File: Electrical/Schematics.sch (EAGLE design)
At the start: 16 parts, among them IC1 3V3, IC2 LM358N, J1 HAN Port, J2 Power Supply (5-12V), T1 BC337

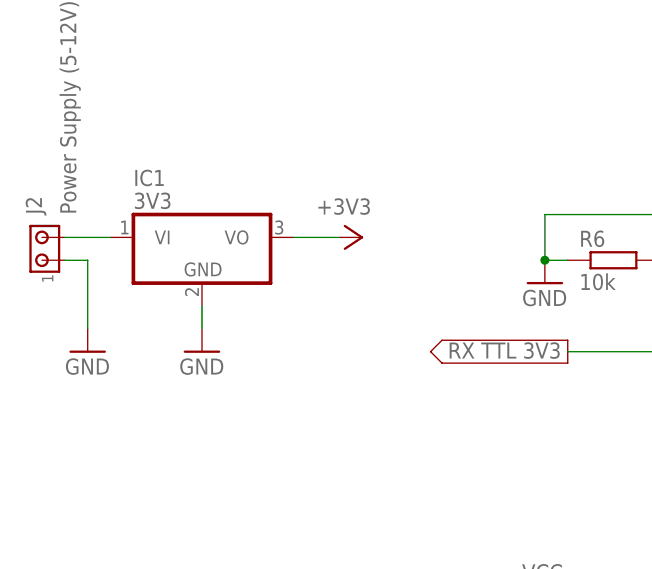
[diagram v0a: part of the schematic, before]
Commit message: Updated with capasitors
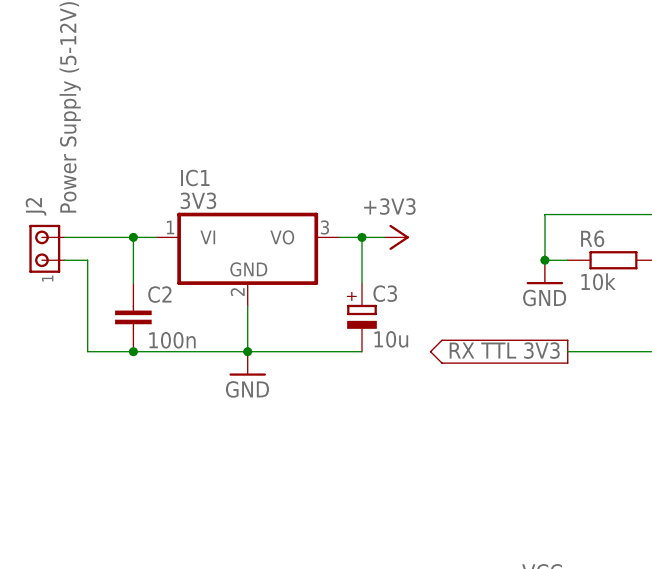
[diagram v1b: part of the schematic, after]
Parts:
- added C2: 100n, resistor:C-EU025-040X050
- added C3: 10u, resistor:CPOL-EUB45181A
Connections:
- net +3V3: now also C3.+
- net GND: now also C2.2, C3.-
- net N$4: now also C2.1
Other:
- moved on the sheet: IC1
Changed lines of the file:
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@@
 <grid distance="0.1" unitdist="inch" unit="inch" style="lines" multiple="1" display="no" altdistance="0.01" altunitdist="inch" altunit="inch"/>
 <layers>
-<layer number="1" name="Top" color="4" fill="1" visible="yes" active="no"/>
-<layer number="16" name="Bottom" color="1" fill="1" visible="yes" active="no"/>
-<layer number="17" name="Pads" color="2" fill="1" visible="yes" active="no"/>
-<layer number="18" name="Vias" color="2" fill="1" visible="yes" active="no"/>
-<layer number="19" name="Unrouted" color="6" fill="1" visible="yes" active="no"/>
-<layer number="20" name="Dimension" color="15" fill="1" visible="yes" active="no"/>
-<layer number="21" name="tPlace" color="7" fill="9" visible="yes" active="no"/>
-<layer number="22" name="bPlace" color="7" fill="1" visible="yes" active="no"/>
-<layer number="23" name="tOrigins" color="15" fill="1" visible="yes" active="no"/>
-<layer number="24" name="bOrigins" color="15" fill="1" visible="yes" active="no"/>
-<layer number="25" name="tNames" color="7" fill="1" visible="yes" active="no"/>
-<layer number="26" name="bNames" color="7" fill="1" visible="yes" active="no"/>
-<layer number="27" name="tValues" color="7" fill="1" visible="yes" active="no"/>
-<layer number="28" name="bValues" color="7" fill="1" visible="yes" active="no"/>
+<layer number="1" name="Top" color="4" fill="1" visible="no" active="no"/>
+<layer number="16" name="Bottom" color="1" fill="1" visible="no" active="no"/>
+<layer number="17" name="Pads" color="2" fill="1" visible="no" active="no"/>
+<layer number="18" name="Vias" color="2" fill="1" visible="no" active="no"/>
+<layer number="19" name="Unrouted" color="6" fill="1" visible="no" active="no"/>
+<layer number="20" name="Dimension" color="15" fill="1" visible="no" active="no"/>
+<layer number="21" name="tPlace" color="7" fill="9" visible="no" active="no"/>
+<layer number="22" name="bPlace" color="7" fill="1" visible="no" active="no"/>
+<layer number="23" name="tOrigins" color="15" fill="1" visible="no" active="no"/>
+<layer number="24" name="bOrigins" color="15" fill="1" visible="no" active="no"/>
+<layer number="25" name="tNames" color="7" fill="1" visible="no" active="no"/>
+<layer number="26" name="bNames" color="7" fill="1" visible="no" active="no"/>
+<layer number="27" name="tValues" color="7" fill="1" visible="no" active="no"/>
+<layer number="28" name="bValues" color="7" fill="1" visible="no" active="no"/>
 <layer number="29" name="tStop" color="7" fill="3" visible="no" active="no"/>
 <layer number="30" name="bStop" color="7" fill="6" visible="no" active="no"/>
@@
 <layer number="35" name="tGlue" color="7" fill="4" visible="no" active="no"/>
 <layer number="36" name="bGlue" color="7" fill="5" visible="no" active="no"/>
-<layer number="37" name="tTest" color="7" fill="1" visible="yes" active="no"/>
-<layer number="38" name="bTest" color="7" fill="1" visible="yes" active="no"/>
+<layer number="37" name="tTest" color="7" fill="1" visible="no" active="no"/>
+<layer number="38" name="bTest" color="7" fill="1" visible="no" active="no"/>
 <layer number="39" name="tKeepout" color="4" fill="11" visible="no" active="no"/>
 <layer number="40" name="bKeepout" color="1" fill="11" visible="no" active="no"/>
@@
 <layer number="44" name="Drills" color="7" fill="1" visible="no" active="no"/>
 <layer number="45" name="Holes" color="7" fill="1" visible="no" active="no"/>
-<layer number="46" name="Milling" color="3" fill="1" visible="yes" active="no"/>
-<layer number="47" name="Measures" color="7" fill="1" visible="yes" active="no"/>
-<layer number="48" name="Document" color="7" fill="1" visible="yes" active="no"/>
-<layer number="49" name="Reference" color="7" fill="1" visible="yes" active="no"/>
-<layer number="51" name="tDocu" color="6" fill="1" visible="yes" active="no"/>
-<layer number="52" name="bDocu" color="7" fill="1" visible="yes" active="no"/>
+<layer number="46" name="Milling" color="3" fill="1" visible="no" active="no"/>
+<layer number="47" name="Measures" color="7" fill="1" visible="no" active="no"/>
+<layer number="48" name="Document" color="7" fill="1" visible="no" active="no"/>
+<layer number="49" name="Reference" color="7" fill="1" visible="no" active="no"/>
+<layer number="51" name="tDocu" color="6" fill="1" visible="no" active="no"/>
+<layer number="52" name="bDocu" color="7" fill="1" visible="no" active="no"/>
 <layer number="90" name="Modules" color="5" fill="1" visible="yes" active="yes"/>
 <layer number="91" name="Nets" color="2" fill="1" visible="yes" active="yes"/>
@@
 <part name="GND4" library="supply1" deviceset="GND" device=""/>
 <part name="GND5" library="supply1" deviceset="GND" device=""/>
-<part name="GND6" library="supply1" deviceset="GND" device=""/>
 <part name="U$1" library="esp8266modules" deviceset="ESP12" device=""/>
 <part name="IC1" library="linear" deviceset="78*" device="TV" technology="05" value="3V3"/>
@@
 <part name="RX3V3" library="supply2" deviceset="V--&gt;" device="" value="RX TTL 3V3"/>
 <part name="SUPPLY3" library="supply2" deviceset="V&lt;--" device="" value="RX TTL 3V3"/>
+<part name="C2" library="resistor" deviceset="C-EU" device="025-040X050" value="100n"/>
+<part name="C3" library="resistor" deviceset="CPOL-EU" device="B45181A" value="10u"/>
 </parts>
 <sheets>
@@
 <instance part="GND2" gate="1" x="-17.78" y="35.56"/>
 <instance part="GND3" gate="1" x="17.78" y="35.56"/>
-<instance part="GND4" gate="1" x="-7.62" y="106.68"/>
+<instance part="GND4" gate="1" x="-2.54" y="104.14"/>
 <instance part="GND5" gate="1" x="60.96" y="35.56"/>
-<instance part="GND6" gate="1" x="-20.32" y="106.68"/>
 <instance part="U$1" gate="G$1" x="60.96" y="111.76" rot="R180"/>
-<instance part="IC1" gate="A1" x="-7.62" y="119.38"/>
+<instance part="IC1" gate="A1" x="-2.54" y="119.38"/>
 <instance part="IC2" gate="A" x="30.48" y="55.88"/>
-<instance part="+3V1" gate="G$1" x="10.16" y="119.38" rot="R270"/>
+<instance part="+3V1" gate="G$1" x="15.24" y="119.38" rot="R270"/>
 <instance part="P+2" gate="VCC" x="30.48" y="78.74" rot="R270"/>
 <instance part="+3V2" gate="G$1" x="60.96" y="81.28"/>
@@
 <instance part="RX3V3" gate="G$1" x="71.12" y="60.96"/>
 <instance part="SUPPLY3" gate="G$1" x="33.02" y="106.68"/>
+<instance part="C2" gate="G$1" x="-15.24" y="111.76"/>
+<instance part="C3" gate="G$1" x="10.16" y="111.76"/>
 </instances>
 <busses>
@@
 <pinref part="IC1" gate="A1" pin="GND"/>
 <pinref part="GND4" gate="1" pin="GND"/>
-<wire x1="-7.62" y1="111.76" x2="-7.62" y2="109.22" width="0.1524" layer="91"/>
-</segment>
-<segment>
+<wire x1="-2.54" y1="111.76" x2="-2.54" y2="106.68" width="0.1524" layer="91"/>
 <pinref part="J2" gate="G$1" pin="1"/>
-<pinref part="GND6" gate="1" pin="GND"/>
 <wire x1="-22.86" y1="116.84" x2="-20.32" y2="116.84" width="0.1524" layer="91"/>
-<wire x1="-20.32" y1="116.84" x2="-20.32" y2="109.22" width="0.1524" layer="91"/>
+<wire x1="-20.32" y1="116.84" x2="-20.32" y2="106.68" width="0.1524" layer="91"/>
+<pinref part="C3" gate="G$1" pin="-"/>
+<wire x1="10.16" y1="106.68" x2="-2.54" y2="106.68" width="0.1524" layer="91"/>
+<pinref part="C2" gate="G$1" pin="2"/>
+<junction x="-15.24" y="106.68"/>
+<wire x1="-2.54" y1="106.68" x2="-15.24" y2="106.68" width="0.1524" layer="91"/>
+<wire x1="-15.24" y1="106.68" x2="-20.32" y2="106.68" width="0.1524" layer="91"/>
+<junction x="-2.54" y="106.68"/>
 </segment>
 <segment>
@@
 <pinref part="J2" gate="G$1" pin="2"/>
 <pinref part="IC1" gate="A1" pin="VI"/>
-<wire x1="-22.86" y1="119.38" x2="-17.78" y2="119.38" width="0.1524" layer="91"/>
+<wire x1="-22.86" y1="119.38" x2="-15.24" y2="119.38" width="0.1524" layer="91"/>
+<pinref part="C2" gate="G$1" pin="1"/>
+<wire x1="-15.24" y1="119.38" x2="-12.7" y2="119.38" width="0.1524" layer="91"/>
+<wire x1="-15.24" y1="114.3" x2="-15.24" y2="119.38" width="0.1524" layer="91"/>
+<junction x="-15.24" y="119.38"/>
 </segment>
 </net>
@@
 <pinref part="IC1" gate="A1" pin="VO"/>
 <pinref part="+3V1" gate="G$1" pin="+3V3"/>
-<wire x1="2.54" y1="119.38" x2="7.62" y2="119.38" width="0.1524" layer="91"/>
-</segment>
-<segment>
+<wire x1="7.62" y1="119.38" x2="10.16" y2="119.38" width="0.1524" layer="91"/>
+<pinref part="C3" gate="G$1" pin="+"/>
+<wire x1="10.16" y1="119.38" x2="12.7" y2="119.38" width="0.1524" layer="91"/>
+<wire x1="10.16" y1="114.3" x2="10.16" y2="119.38" width="0.1524" layer="91"/>
+<junction x="10.16" y="119.38"/>
+</segment>
+<segment>
